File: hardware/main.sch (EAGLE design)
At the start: 39 parts, among them U1 TMS320F28069_PN_80, U10 TXB0101_DBV_6, U2 TXB0101_DBV_6, U3 TS3A5018_PW_16, U4 TS3A5018_PW_16, U5 SN74LVC4245A_DW_24, U7 Value, U8 Value, U9 SN74LVC4245A_DW_24

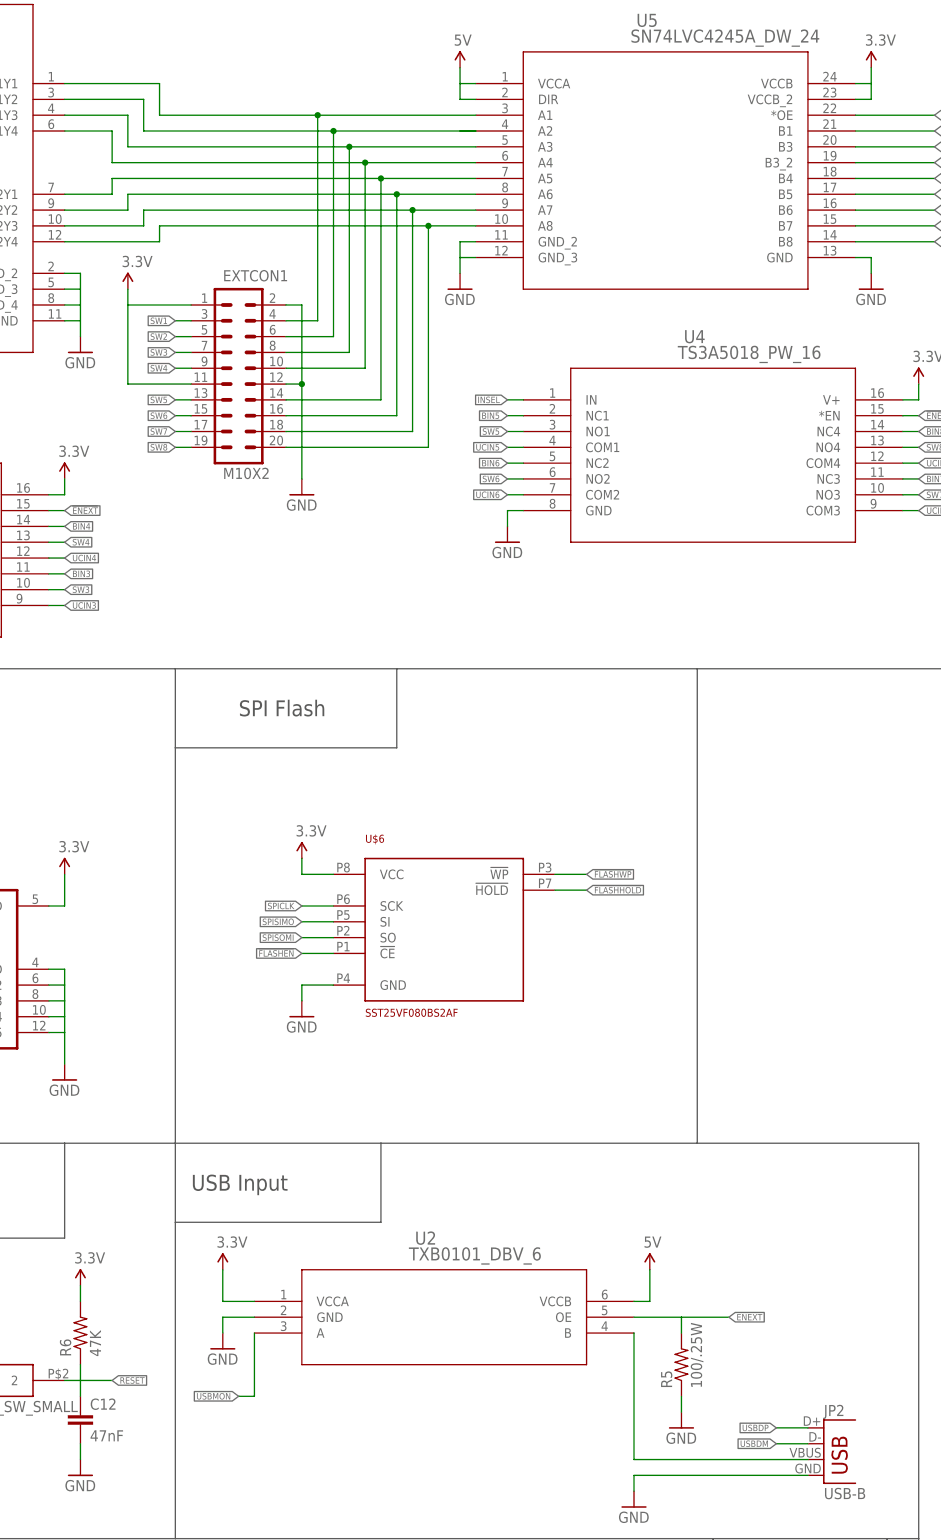
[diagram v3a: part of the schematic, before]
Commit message: Updated input ribbon connector schematic, began to route input analog switches
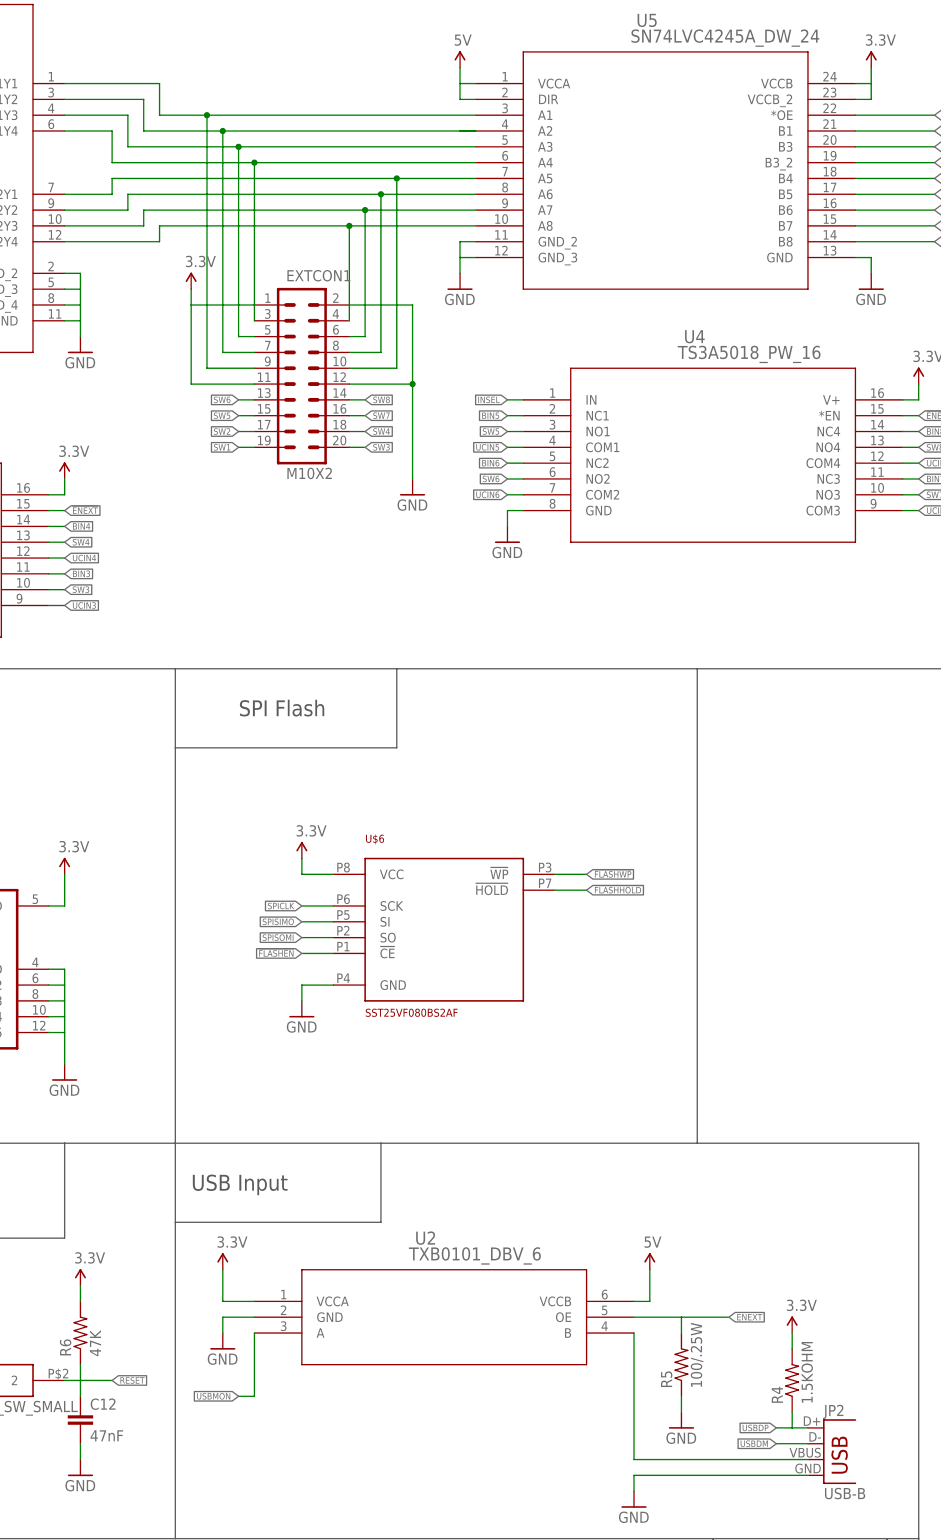
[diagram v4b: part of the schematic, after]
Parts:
- added R4: 1.5KOHM, SparkFun-Resistors:1.5KOHM-1/10W-1%(0603)
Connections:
- net 3.3V: now also R4.2
- net IBUFOUT1: now also EXTCON1.9; no longer EXTCON1.4
- net IBUFOUT2: now also EXTCON1.7; no longer EXTCON1.6
- net IBUFOUT3: now also EXTCON1.5; no longer EXTCON1.8
- net IBUFOUT4: now also EXTCON1.3; no longer EXTCON1.10
- net IBUFOUT5: now also EXTCON1.10; no longer EXTCON1.14
- net IBUFOUT6: now also EXTCON1.8; no longer EXTCON1.16
- net IBUFOUT7: now also EXTCON1.6; no longer EXTCON1.18
- net IBUFOUT8: now also EXTCON1.4; no longer EXTCON1.20
- net SW1: now also EXTCON1.19; no longer EXTCON1.3
- net SW2: now also EXTCON1.17; no longer EXTCON1.5
- net SW3: now also EXTCON1.20; no longer EXTCON1.7
- net SW4: now also EXTCON1.18; no longer EXTCON1.9
- net SW5: now also EXTCON1.15; no longer EXTCON1.13
- net SW6: now also EXTCON1.13; no longer EXTCON1.15
- net SW7: now also EXTCON1.16; no longer EXTCON1.17
- net SW8: now also EXTCON1.14; no longer EXTCON1.19
- net USBDP: now also R4.1
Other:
- moved on the sheet: EXTCON1

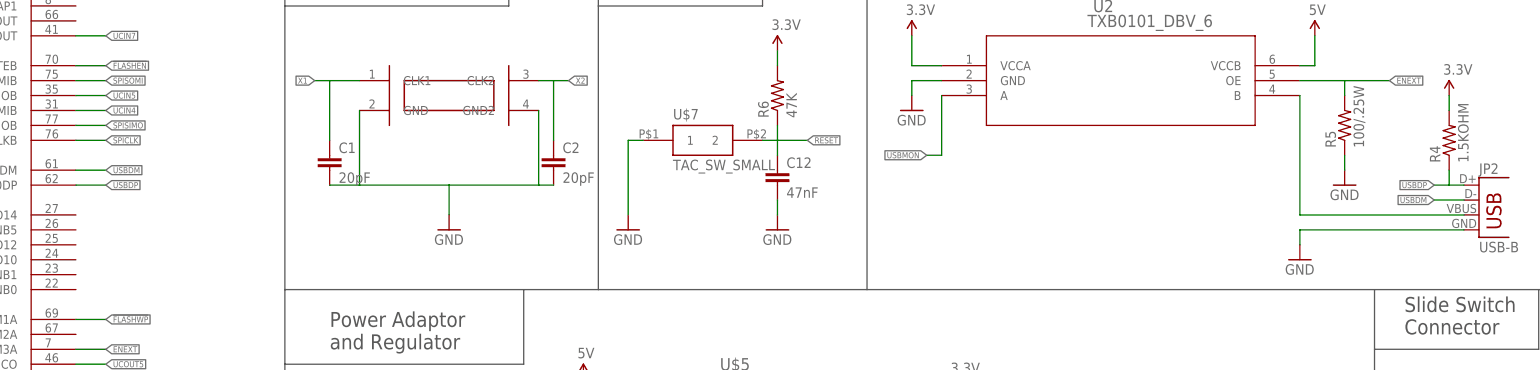
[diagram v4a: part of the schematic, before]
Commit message: Ripped up USB routing, SPI routing, and previously made input stage routing. Starting over.
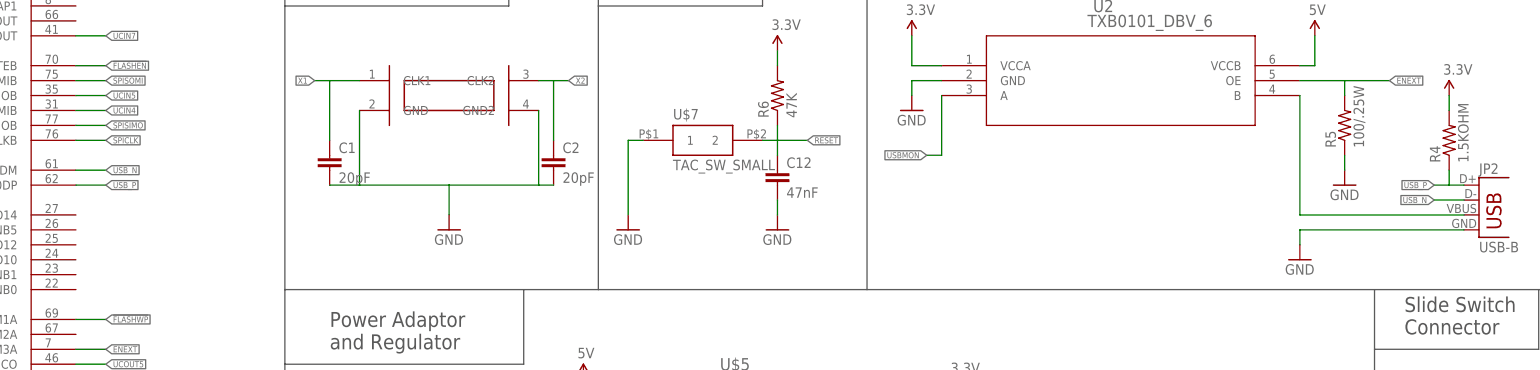
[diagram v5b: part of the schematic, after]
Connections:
- net USBDM renamed USB_N
- net USBDP renamed USB_P
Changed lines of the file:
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@@
-</segment>
-</net>
-<net name="USBDM" class="0">
-<segment>
-<pinref part="U1" gate="A" pin="GPIO27/HRCAP2/*SPISTEB/USB0DM"/>
-<wire x1="228.6" y1="66.04" x2="233.68" y2="66.04" width="0.1524" layer="91"/>
-<label x="233.68" y="66.04" size="1.016" layer="95" xref="yes"/>
-</segment>
-<segment>
-<pinref part="JP2" gate="G$1" pin="D-"/>
-<wire x1="464.82" y1="60.96" x2="459.74" y2="60.96" width="0.1524" layer="91"/>
-<label x="459.74" y="60.96" size="1.016" layer="95" rot="R180" xref="yes"/>
-</segment>
-</net>
-<net name="USBDP" class="0">
-<segment>
-<pinref part="U1" gate="A" pin="GPIO26/ECAP3/SPICLKB/USB0DP"/>
-<wire x1="228.6" y1="63.5" x2="233.68" y2="63.5" width="0.1524" layer="91"/>
-<label x="233.68" y="63.5" size="1.016" layer="95" xref="yes"/>
-</segment>
-<segment>
-<pinref part="JP2" gate="G$1" pin="D+"/>
-<wire x1="464.82" y1="63.5" x2="462.28" y2="63.5" width="0.1524" layer="91"/>
-<label x="459.74" y="63.5" size="1.016" layer="95" rot="R180" xref="yes"/>
-<pinref part="R4" gate="G$1" pin="1"/>
-<wire x1="462.28" y1="63.5" x2="459.74" y2="63.5" width="0.1524" layer="91"/>
-<wire x1="462.28" y1="66.04" x2="462.28" y2="63.5" width="0.1524" layer="91"/>
 </segment>
 </net>
@@
 </segment>
 </net>
+<net name="USB_N" class="0">
+<segment>
+<pinref part="U1" gate="A" pin="GPIO27/HRCAP2/*SPISTEB/USB0DM"/>
+<wire x1="228.6" y1="66.04" x2="233.68" y2="66.04" width="0.1524" layer="91"/>
+<label x="233.68" y="66.04" size="1.016" layer="95" xref="yes"/>
+</segment>
+<segment>
+<pinref part="JP2" gate="G$1" pin="D-"/>
+<wire x1="464.82" y1="60.96" x2="459.74" y2="60.96" width="0.1524" layer="91"/>
+<label x="459.74" y="60.96" size="1.016" layer="95" rot="R180" xref="yes"/>
+</segment>
+</net>
+<net name="USB_P" class="0">
+<segment>
+<pinref part="U1" gate="A" pin="GPIO26/ECAP3/SPICLKB/USB0DP"/>
+<wire x1="228.6" y1="63.5" x2="233.68" y2="63.5" width="0.1524" layer="91"/>
+<label x="233.68" y="63.5" size="1.016" layer="95" xref="yes"/>
+</segment>
+<segment>
+<pinref part="JP2" gate="G$1" pin="D+"/>
+<wire x1="464.82" y1="63.5" x2="462.28" y2="63.5" width="0.1524" layer="91"/>
+<label x="459.74" y="63.5" size="1.016" layer="95" rot="R180" xref="yes"/>
+<pinref part="R4" gate="G$1" pin="1"/>
+<wire x1="462.28" y1="63.5" x2="459.74" y2="63.5" width="0.1524" layer="91"/>
+<wire x1="462.28" y1="66.04" x2="462.28" y2="63.5" width="0.1524" layer="91"/>
+</segment>
+</net>

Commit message: Change analog switch for input selection to buffer. Reviewed and reworked enable pin logic. Added single NOT gate and 5V buffer to ControllerCard library
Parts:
- removed EXTCON3: (no value), SparkFun-Connectors:M04PTH
- added JP4: (no value), SparkFun-Connectors:M05PTH
- U3: value TS3A5018_PW_16 -> SN74ABT541B_DW_20; device ControllerCard:TS3A5018_PW_16 -> ControllerCard:SN74ABT541B_DW_20
- U4: value TS3A5018_PW_16 -> SN74LVC1G04_DBV_5; device ControllerCard:TS3A5018_PW_16 -> ControllerCard:SN74LVC1G04_DBV_5
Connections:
- removed net SW1: EXTCON1.19, U3.NO1
- removed net SW2: EXTCON1.17, U3.NO2
- removed net SW3: EXTCON1.20, U3.NO3
- removed net SW4: EXTCON1.18, U3.NO4
- removed net SW5: EXTCON1.15, U4.NO1
- removed net SW6: EXTCON1.13, U4.NO2
- removed net SW7: EXTCON1.16, U4.NO3
- removed net SW8: EXTCON1.14, U4.NO4
- new net !INSEL!: U3.*OE1, U3.*OE2, U4.Y
- new net N$29: EXTCON1.4, U3.A1
- new net N$30: EXTCON1.6, U3.A2
- new net N$31: EXTCON1.8, U3.A3
- new net N$32: EXTCON1.10, U3.A4
- new net N$33: EXTCON1.12, U3.A5
- new net N$34: EXTCON1.14, U3.A6
- new net N$35: EXTCON1.16, U3.A7
- new net N$36: EXTCON1.18, U3.A8
- net !BUFEN!: no longer U7.1OE_N, U7.2OE_N
- net !ENEXT!: no longer U3.*EN, U4.*EN
- net 3.3V: now also JP4.4; no longer EXTCON1.1, EXTCON1.11, EXTCON3.4, U3.V+, U4.V+
- net 5V: now also EXTCON1.1, EXTCON1.19, JP4.5, U3.VCC, U4.VCC
- net BIN1: no longer U3.NC1
- net BIN2: no longer U3.NC2
- net BIN3: no longer U3.NC3
- net BIN4: no longer U3.NC4
- net BIN5: no longer U4.NC1
- net BIN6: no longer U4.NC2
- net BIN7: no longer U4.NC3
- net BIN8: no longer U4.NC4
- net GND: now also EXTCON1.20, JP4.1; no longer EXTCON1.12, EXTCON3.1
- net IBUFOUT1: now also EXTCON1.3, U3.Y1; no longer EXTCON1.9
- net IBUFOUT2: now also EXTCON1.5, U3.Y2; no longer EXTCON1.7
- net IBUFOUT3: now also EXTCON1.7, U3.Y3; no longer EXTCON1.5
- net IBUFOUT4: now also EXTCON1.9, U3.Y4; no longer EXTCON1.3
- net IBUFOUT5: now also EXTCON1.11, U3.Y5; no longer EXTCON1.10
- net IBUFOUT6: now also EXTCON1.13, U3.Y6; no longer EXTCON1.8
- net IBUFOUT7: now also EXTCON1.15, U3.Y7; no longer EXTCON1.6
- net IBUFOUT8: now also EXTCON1.17, U3.Y8; no longer EXTCON1.4
- net INSEL: now also JP4.3, U4.A, U7.1OE_N, U7.2OE_N; no longer EXTCON3.3, U3.IN, U4.IN
- net RUNSEL: now also JP4.2; no longer EXTCON3.2
- net UCIN1: no longer U3.COM1
- net UCIN2: no longer U3.COM2
- net UCIN3: no longer U3.COM3
- net UCIN4: no longer U3.COM4
- net UCIN5: no longer U4.COM1
- net UCIN6: no longer U4.COM2
- net UCIN7: no longer U4.COM3
- net UCIN8: no longer U4.COM4
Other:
- moved on the sheet: EXTCON1, U5

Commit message: Finished routing part of the board. Rearranged input connector in schematic.
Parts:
- removed EXTCON1: M10X2, SparkFun-Connectors:M10X2
- added LEDCON, SWCON: M05X2PTH, SparkFun-Connectors:M05X2PTH
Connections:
- removed net BIN1: U5.B1
- removed net BIN2: U5.B3
- removed net BIN3: U5.B3_2
- removed net BIN4: U5.B4
- removed net BIN5: U5.B5
- removed net BIN6: U5.B6
- removed net BIN7: U5.B7
- removed net BIN8: U5.B8
- new net N$37: SWCON.8, U3.A8
- net !FLASHEN!: now also U1.GPIO33/SCLA/EPWMSYNCO/*ADCSOCBO; no longer U1.GPIO15/ECAP2/SCIRXDB/*SPISTEB
- net !FLASHWP!: now also U1.GPIO32/SDAA/EPWMSYNCI/*ADCSOCAO; no longer U1.GPIO0/EPWM1A
- net 5V: now also LEDCON.9, SWCON.9; no longer EXTCON1.1, EXTCON1.19
- net GND: now also LEDCON.10; no longer EXTCON1.2, EXTCON1.20
- net IBUFOUT1: now also LEDCON.1; no longer EXTCON1.3
- net IBUFOUT2: now also LEDCON.3; no longer EXTCON1.5
- net IBUFOUT3: now also LEDCON.5; no longer EXTCON1.7
- net IBUFOUT4: now also LEDCON.7; no longer EXTCON1.9
- net IBUFOUT5: now also LEDCON.2; no longer EXTCON1.11
- net IBUFOUT6: now also LEDCON.4; no longer EXTCON1.13
- net IBUFOUT7: now also LEDCON.6; no longer EXTCON1.15
- net IBUFOUT8: now also LEDCON.8; no longer EXTCON1.17
- net N$17: now also U$4.8; no longer U$4.5
- net N$18: now also U$4.7; no longer U$4.6
- net N$19: now also U$4.6; no longer U$4.7
- net N$20: now also U$4.5; no longer U$4.8
- net N$21: now also U$8.8; no longer U$8.1
- net N$22: now also U$8.7; no longer U$8.2
- net N$23: now also U$8.6; no longer U$8.3
- net N$24: now also U$8.5; no longer U$8.4
- net N$25: now also U$8.1; no longer U$8.8
- net N$26: now also U$8.2; no longer U$8.7
- net N$27: now also U$8.3; no longer U$8.6
- net N$28: now also U$8.4; no longer U$8.5
- net N$29: now also SWCON.1; no longer EXTCON1.4
- net N$30: now also SWCON.3; no longer EXTCON1.6
- net N$31: now also SWCON.5; no longer EXTCON1.8
- net N$32: now also SWCON.7; no longer EXTCON1.10
- net N$33: now also SWCON.2; no longer EXTCON1.12
- net N$34: now also SWCON.4; no longer EXTCON1.14
- net N$35: now also SWCON.6; no longer EXTCON1.16
- net N$36: now also SWCON.10; no longer EXTCON1.18, U3.A8
- net UCIN1: now also U1.GPIO25/ECAP2/SPISOMIB, U5.B1; no longer U1.GPIO30/CANRXA/EPWM7A
- net UCIN2: now also U1.GPIO31/CANTXA/EPWM8A, U5.B3; no longer U1.GPIO29/SCITXDA/SCLA/*TZ3
- net UCIN3: now also U1.GPIO30/CANRXA/EPWM7A, U5.B3_2; no longer U1.GPIO31/CANTXA/EPWM8A
- net UCIN4: now also U1.GPIO29/SCITXDA/SCLA/*TZ3, U5.B4; no longer U1.GPIO25/ECAP2/SPISOMIB
- net UCIN5: now also U5.B5
- net UCIN6: now also U5.B6
- net UCIN7: now also U1.GPIO28/SCIRXDA/SDAA/*TZ2, U5.B7; no longer U1.GPIO18/SPICLKA/SCITXDB/XCLKOUT
- net UCIN8: now also U1.GPIO18/SPICLKA/SCITXDB/XCLKOUT, U5.B8; no longer U1.GPIO28/SCIRXDA/SDAA/*TZ2

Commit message: Changed ribbon cable connectors to components on the board. Added DIP switch, LED's. Re-arranged components, started routing.
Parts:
- removed JP3: M10SILK_FEMALE_PTH, SparkFun-Connectors:M10SILK_FEMALE_PTH
- removed LEDCON, SWCON: M05X2PTH, SparkFun-Connectors:M05X2PTH
- added D1, D10, D11, D12, D13, D14, D15, D16, D2, D3, D4, D5, D6, D7, D8, D9: (no value), SparkFun-LED:LED3MM
- added R10, R11, R12, R13, R14, R15, R16, R17, R18, R19, R20, R21, R22, R23, R8, R9: 240, SparkFun-Resistors:240OHM1/10W1%(0603)
- added R24, R25, R26, R27, R28, R29, R30, R31: 10K, SparkFun-Resistors:10KOHM-1/10W-1%(0603)0603
- added U$9: 8BIT-DIP-SWITCH, ControllerCard:8BIT-DIP-SWITCH
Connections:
- removed net IBUFOUT1: LEDCON.1, U3.Y1, U5.A1, U7.1Y1
- removed net IBUFOUT2: LEDCON.3, U3.Y2, U5.A2, U7.1Y2
- removed net IBUFOUT3: LEDCON.5, U3.Y3, U5.A3, U7.1Y3
- removed net IBUFOUT4: LEDCON.7, U3.Y4, U5.A4, U7.1Y4
- removed net IBUFOUT5: LEDCON.2, U3.Y5, U5.A5, U7.2Y1
- removed net IBUFOUT6: LEDCON.4, U3.Y6, U5.A6, U7.2Y2
- removed net IBUFOUT7: LEDCON.6, U3.Y7, U5.A7, U7.2Y3
- removed net IBUFOUT8: LEDCON.8, U3.Y8, U5.A8, U7.2Y4
- removed net N$29: SWCON.1, U3.A1
- new net LEDIN1: R16.2, U3.Y1, U5.A1, U7.1Y1
- new net LEDIN2: R17.2, U3.Y2, U5.A2, U7.1Y2
- new net LEDIN3: R18.2, U3.Y3, U5.A3, U7.1Y3
- new net LEDIN4: R19.2, U3.Y4, U5.A4, U7.1Y4
- new net LEDIN5: R20.2, U3.Y5, U5.A5, U7.2Y1
- new net LEDIN6: R21.2, U3.Y6, U5.A6, U7.2Y2
- new net LEDIN7: R22.2, U3.Y7, U5.A7, U7.2Y3
- new net LEDIN8: R23.2, U3.Y8, U5.A8, U7.2Y4
- new net LEDOUT1: R8.2, U8.1A1, U9.A1
- new net LEDOUT2: R9.2, U8.1A2, U9.A2
- new net LEDOUT3: R10.2, U8.1A3, U9.A3
- new net LEDOUT4: R11.2, U8.1A4, U9.A4
- new net LEDOUT5: R12.2, U8.2A1, U9.A5
- new net LEDOUT6: R13.2, U8.2A2, U9.A6
- new net LEDOUT7: R14.2, U8.2A3, U9.A7
- new net LEDOUT8: R15.2, U8.2A4, U9.A8
- new net SW1: R24.2, U$9.IN1, U3.A1
- new net SW2: R25.2, U$9.IN2, U3.A2
- new net SW3: R26.2, U$9.IN3, U3.A3
- new net SW4: R27.2, U$9.IN4, U3.A4
- new net SW5: R28.2, U$9.IN5, U3.A5
- new net SW6: R29.2, U$9.IN6, U3.A6
- new net SW7: R30.2, U$9.IN7, U3.A7
- new net SW8: R31.2, U$9.IN8, U3.A8
- net 5V: now also U$9.CL1, U$9.CL2, U$9.CL3, U$9.CL4, U$9.CL5, U$9.CL6, U$9.CL7, U$9.CL8; no longer JP3.10, LEDCON.9, SWCON.9
- net GND: now also D1.C, D10.C, D11.C, D12.C, D13.C, D14.C, D15.C, D16.C, D2.C, D3.C, D4.C, D5.C, D6.C, D7.C, D8.C, D9.C, R24.1, R25.1, R26.1, R27.1, R28.1, R29.1, R30.1, R31.1; no longer JP3.1, LEDCON.10
- net N$10: now also D6.A, R13.1; no longer JP3.8, U8.2A3, U9.A7
- net N$11: now also D7.A, R14.1; no longer JP3.7, U8.2A2, U9.A6
- net N$12: now also D8.A, R15.1; no longer JP3.6, U8.2A1, U9.A5
- net N$30: now also D9.A, R16.1; no longer SWCON.3, U3.A2
- net N$31: now also D10.A, R17.1; no longer SWCON.5, U3.A3
- net N$32: now also D11.A, R18.1; no longer SWCON.7, U3.A4
- net N$33: now also D12.A, R19.1; no longer SWCON.2, U3.A5
- net N$34: now also D13.A, R20.1; no longer SWCON.4, U3.A6
- net N$35: now also D14.A, R21.1; no longer SWCON.6, U3.A7
- net N$36: now also D15.A, R22.1; no longer SWCON.10
- net N$37: now also D16.A, R23.1; no longer SWCON.8, U3.A8
- net N$5: now also D1.A, R8.1; no longer JP3.2, U8.1A1, U9.A1
- net N$6: now also D2.A, R9.1; no longer JP3.3, U8.1A2, U9.A2
- net N$7: now also D3.A, R10.1; no longer JP3.4, U8.1A3, U9.A3
- net N$8: now also D4.A, R11.1; no longer JP3.5, U8.1A4, U9.A4
- net N$9: now also D5.A, R12.1; no longer JP3.9, U8.2A4, U9.A8
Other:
- moved on the sheet: U3, U4, U5
